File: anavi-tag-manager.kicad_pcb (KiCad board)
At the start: 2 copper layers, 74.9 x 40.6 mm, 31 parts, among them P1 CONN_01X03, U1 I2C_SENS_1, U2 I2C_SENS_1, U3 I2C_SENS_1

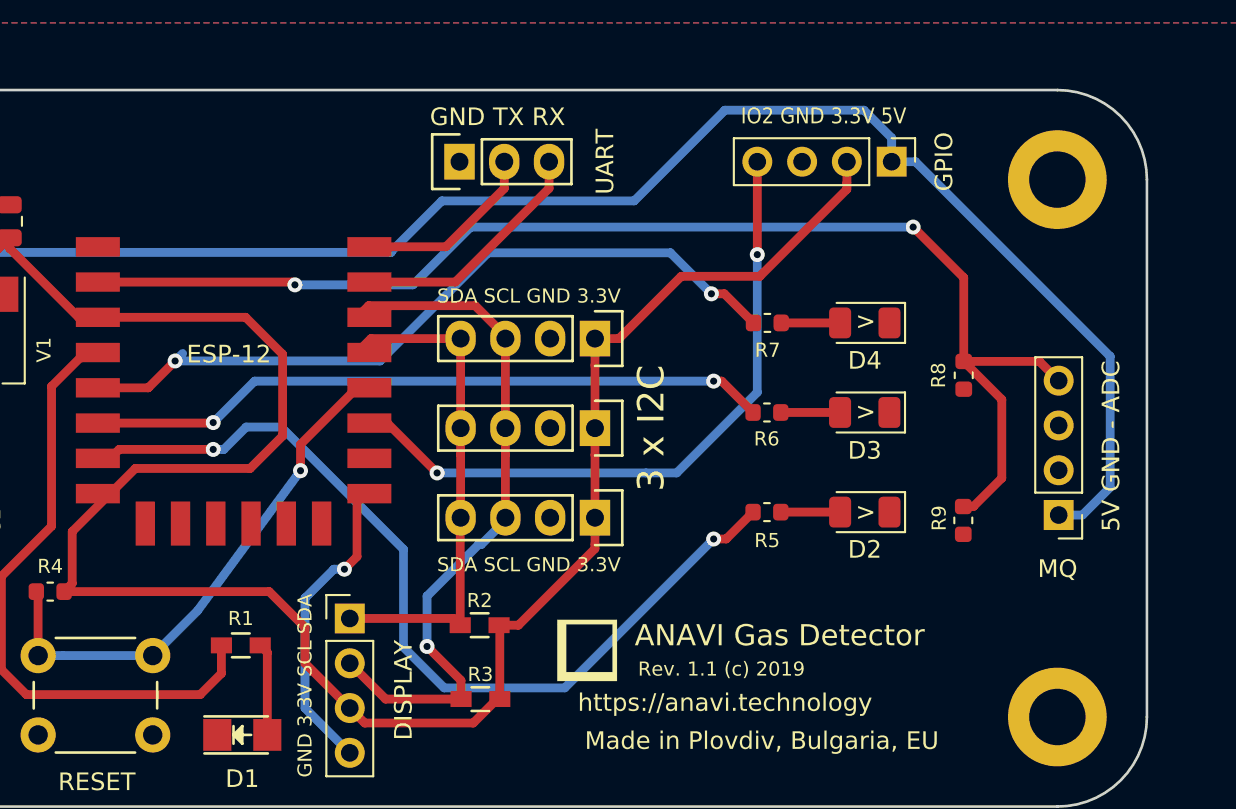
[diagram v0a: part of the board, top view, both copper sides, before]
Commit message: anavi-tag-manager.kicad_pcb: Clear old tracks
Clear old tracks and prepare for net list import.

Signed-off-by: Leon Anavi <leon@anavi.org>
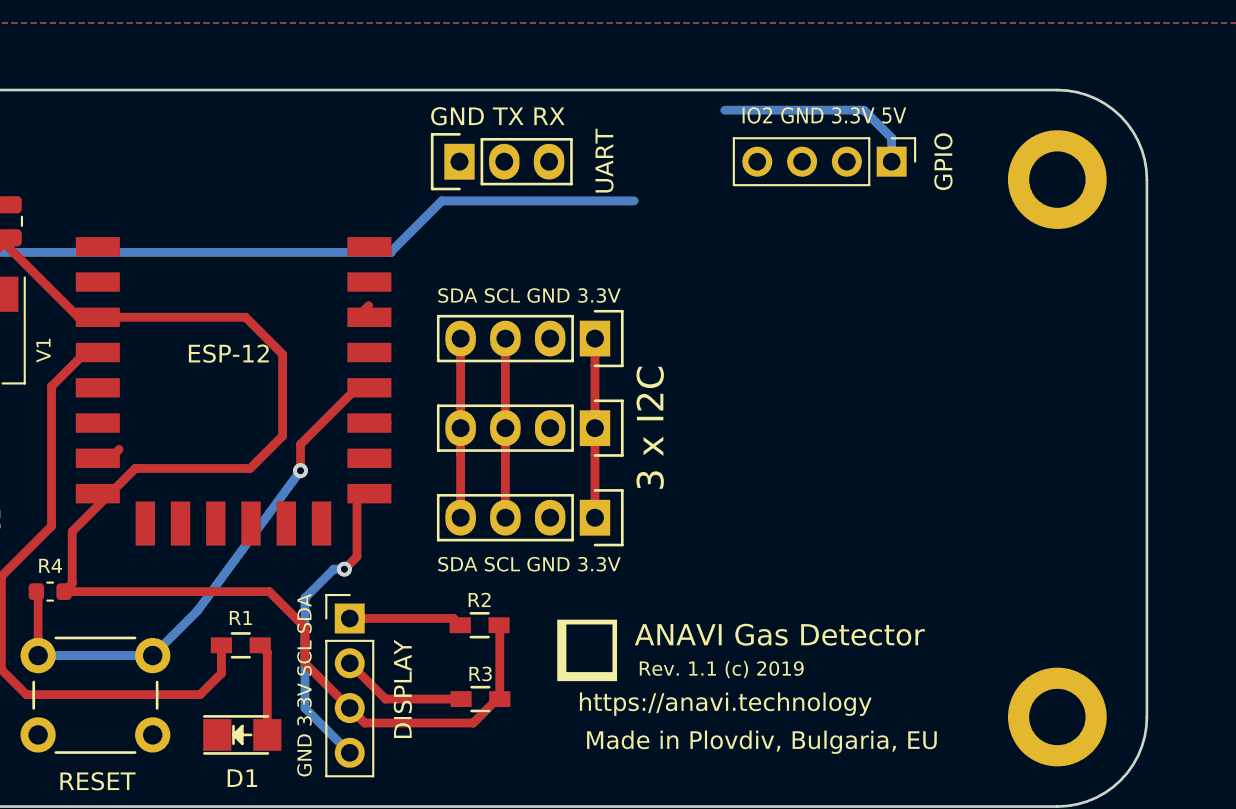
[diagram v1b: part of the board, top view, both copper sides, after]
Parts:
- removed D2: KP-3216SGC, LED_SMD:LED_1206_3216Metric
- removed D3: KP-3216YC, LED_SMD:LED_1206_3216Metric
- removed D4: KP-3216EC, LED_SMD:LED_1206_3216Metric
- removed MQ: Conn_01x04, Connector_PinHeader_2.54mm:PinHeader_1x04_P2.54mm_Vertical
- removed R5, R6, R7: 68R, Resistor_SMD:R_0603_1608Metric
- removed R8: 220K, Resistor_SMD:R_0603_1608Metric
- removed R9: 56K, Resistor_SMD:R_0603_1608Metric
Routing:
- net Net-(ESP-12-Pad2): track 72.0 -> 0.00 mm, vias 2 -> 0
- net Net-(ESP-12-Pad7): track 50.7 -> 0.72 mm, vias 2 -> 0
- net Net-(ESP-12-Pad5): track 41.9 -> 0.00 mm, vias 2 -> 0
- net Net-(ESP-12-Pad6): track 38.2 -> 0.00 mm, vias 2 -> 0
- net Net-(ESP-12-Pad11): track 40.3 -> 3.12 mm, vias 2 -> 0
- net +5V: track 109.3 -> 74.0 mm
- net +3V3: track 118.7 -> 90.3 mm
- net Net-(ESP-12-Pad14): track 39.9 -> 18.5 mm, vias 1 -> 0
- net Net-(ESP-12-Pad15): track 14.6 -> 0.00 mm
- net Net-(ESP-12-Pad13): track 29.9 -> 17.7 mm
- net Net-(ESP-12-Pad16): track 11.2 -> 0.00 mm
- net Net-(D2-Pad2): track 3.36 -> 0.00 mm
- net Net-(D3-Pad2): track 3.36 -> 0.00 mm
- net Net-(D4-Pad2): track 3.34 -> 0.00 mm
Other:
- board text removed: "5V GND - ADC"
- board text removed: ">"

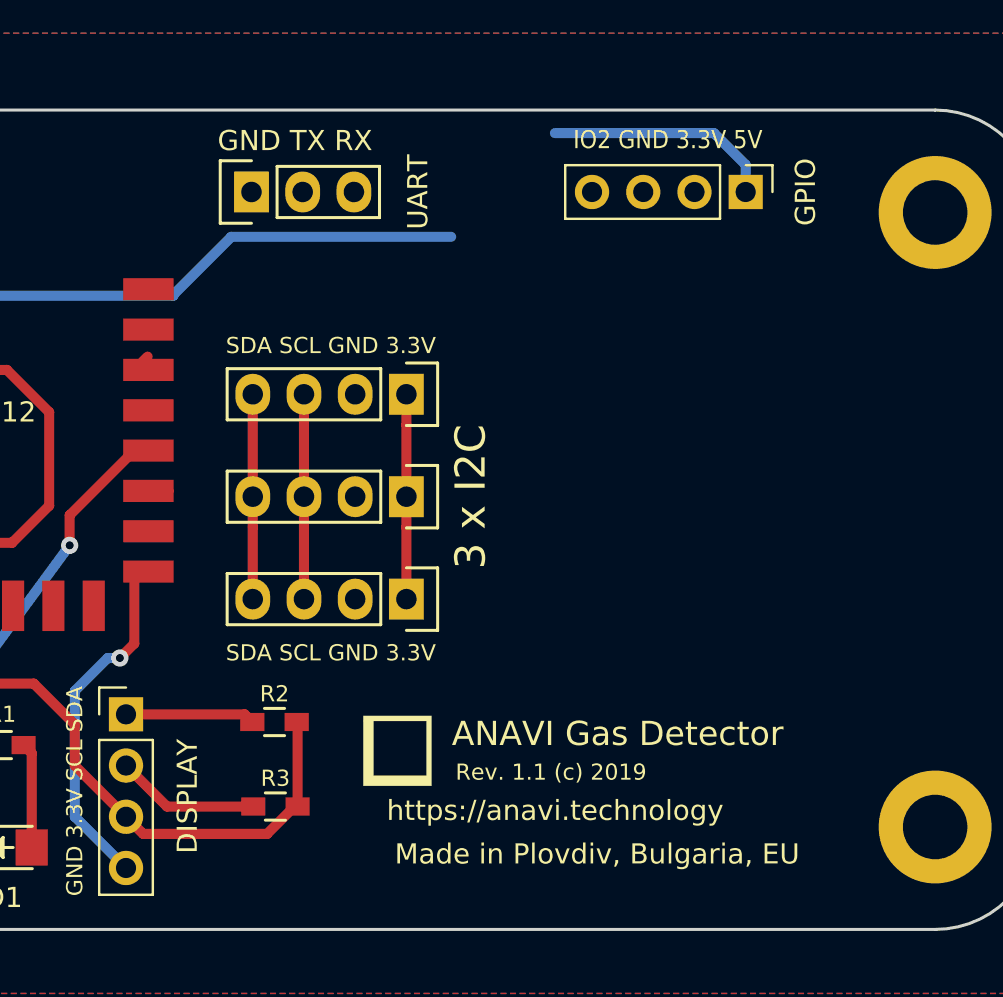
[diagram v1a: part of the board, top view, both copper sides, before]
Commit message: anavi-tag-manager.kicad_pcb: Move components
Move I2C slots and GPIO pins to save some space.

Signed-off-by: Leon Anavi <leon@anavi.org>
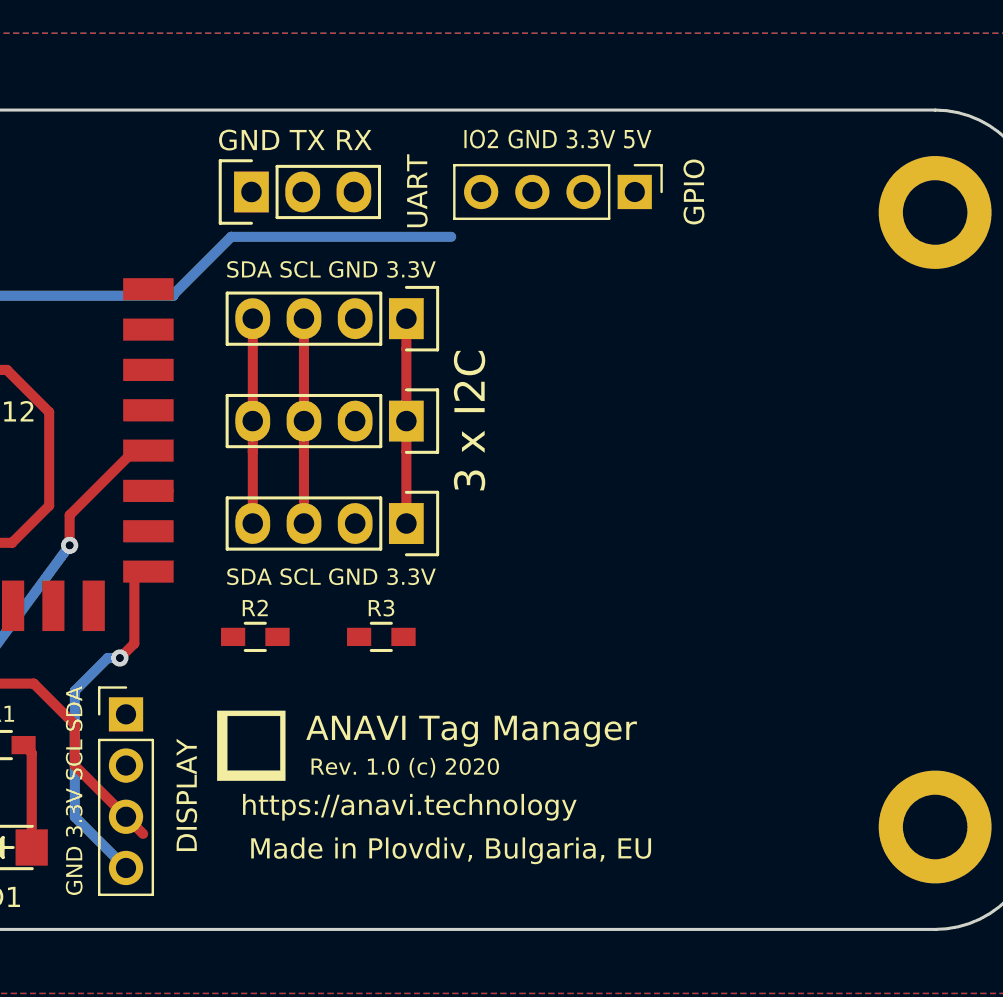
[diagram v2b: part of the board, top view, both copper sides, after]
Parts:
- moved R3 9.92 mm to (107.2, 97.2)
- moved G*** 7.25 mm to (100.7, 102.7)
- moved GPIO 5.50 mm to (119.7, 75.2)
- moved R2 4.33 mm to (100.9, 97.2)
- moved U1 3.75 mm to (108.4, 91.6)
- moved U2 3.75 mm to (108.4, 86.5)
- moved U3 3.75 mm to (108.4, 81.5)
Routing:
- net +3V3: track 90.3 -> 77.9 mm
- net +5V: track 74.0 -> 62.6 mm
- net Net-(ESP-12-Pad14): track 18.5 -> 10.5 mm
- net Net-(ESP-12-Pad13): track 17.7 -> 11.2 mm
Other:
- board text added: "ANAVI Tag Manager"
- board text added: "Rev. 1.0 (c) 2020"
- board text removed: "ANAVI Gas Detector"
- board text removed: "Rev. 1.1 (c) 2019"
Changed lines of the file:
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@@
     (thickness 1.6)
     (drawings 21)
-    (tracks 100)
+    (tracks 87)
     (zones 0)
     (modules 22)
@@
   )
   (setup
-    (last_trace_width 0.5)
+    (last_trace_width 0.254)
     (user_trace_width 0.254)
     (user_trace_width 0.5)
@@
   )
   (module Pin_Headers:Pin_Header_Straight_1x04 (layer F.Cu)
-    (at 108.3945 85.217 270)
+    (at 108.3945 81.467 270)
     (descr "Through hole pin header")
     (tags "pin header")
@@
   )
   (module Resistors_SMD:R_0603_HandSoldering (layer F.Cu)
-    (at 101.854 101.473 180)
+    (at 100.9 97.25 180)
     (descr "Resistor SMD 0603, hand soldering")
     (tags "resistor 0603")
@@
   )
   (module Resistors_SMD:R_0603_HandSoldering (layer F.Cu)
-    (at 101.897 105.664 180)
+    (at 107.15 97.25 180)
     (descr "Resistor SMD 0603, hand soldering")
     (tags "resistor 0603")
@@
   )
   (module Pin_Headers:Pin_Header_Straight_1x04 (layer F.Cu)
-    (at 108.3945 95.377 270)
+    (at 108.3945 91.627 270)
     (descr "Through hole pin header")
     (tags "pin header")
@@
   )
   (module Pin_Headers:Pin_Header_Straight_1x04 (layer F.Cu)
-    (at 108.3945 90.297 270)
+    (at 108.3945 86.547 270)
     (descr "Through hole pin header")
     (tags "pin header")
@@
   )
   (module logo:anavi-logo (layer F.Cu)
-    (at 107.95 102.9462)
+    (at 100.7 102.6962)
     (fp_text reference G*** (at 0 0) (layer F.SilkS) hide
       (effects (font (size 1.524 1.524) (thickness 0.3)))
@@
   )
   (module Connector_PinHeader_2.54mm:PinHeader_1x04_P2.54mm_Vertical (layer F.Cu)
-    (at 125.222 75.184 270)
+    (at 119.722 75.184 270)
     (descr "Through hole straight pin header, 1x04, 2.54mm pitch, single row")
     (tags "Through hole pin header THT 1x04 2.54mm single row")
@@
     )
   )
-  (gr_text "IO2 GND 3.3V 5V" (at 121.3612 72.5932) (layer F.SilkS)
+  (gr_text "IO2 GND 3.3V 5V" (at 115.8612 72.5932) (layer F.SilkS)
     (effects (font (size 0.9 0.8) (thickness 0.15)))
   )
@@
     (effects (font (size 0.8 0.8) (thickness 0.15)))
   )
-  (gr_text "SDA SCL GND 3.3V" (at 104.648 98.044) (layer F.SilkS)
+  (gr_text "SDA SCL GND 3.3V" (at 104.648 94.294) (layer F.SilkS)
     (effects (font (size 0.8 0.8) (thickness 0.15)))
   )
-  (gr_text "SDA SCL GND 3.3V" (at 104.648 82.804) (layer F.SilkS)
+  (gr_text "SDA SCL GND 3.3V" (at 104.648 79.054) (layer F.SilkS)
     (effects (font (size 0.8 0.8) (thickness 0.15)))
   )
@@
     (effects (font (size 1 1) (thickness 0.2)))
   )
-  (gr_text "3 x I2C" (at 111.5822 90.297 90) (layer F.SilkS)
+  (gr_text "3 x I2C" (at 111.5822 86.547 90) (layer F.SilkS)
     (effects (font (size 1.5 1.5) (thickness 0.25)))
   )
@@
     (effects (font (size 1 1) (thickness 0.15)))
   )
-  (gr_text "Made in Plovdiv, Bulgaria, EU" (at 117.856 108.0262) (layer F.SilkS)
+  (gr_text "Made in Plovdiv, Bulgaria, EU" (at 110.606 107.7762) (layer F.SilkS)
     (effects (font (size 1 1) (thickness 0.2)))
   )
-  (gr_text https://anavi.technology (at 115.7732 105.8672) (layer F.SilkS)
+  (gr_text https://anavi.technology (at 108.5232 105.6172) (layer F.SilkS)
     (effects (font (size 1 1) (thickness 0.15)))
   )
-  (gr_text "Rev. 1.1 (c) 2019" (at 115.57 103.9622) (layer F.SilkS)
+  (gr_text "Rev. 1.0 (c) 2020" (at 108.32 103.7122) (layer F.SilkS)
     (effects (font (size 0.8 0.8) (thickness 0.15)))
   )
-  (gr_text "ANAVI Gas Detector" (at 118.872 102.0572) (layer F.SilkS)
+  (gr_text "ANAVI Tag Manager" (at 111.622 101.8072) (layer F.SilkS)
     (effects (font (size 1.2 1.2) (thickness 0.25)))
   )
@@
   (segment (start 91.948 106.172) (end 94.488 108.712) (width 0.5) (layer B.Cu) (net 2))
   (segment (start 91.948 99.93216) (end 91.948 106.172) (width 0.5) (layer B.Cu) (net 2))
-  (segment (start 108.288 85.1105) (end 108.3945 85.217) (width 0.5) (layer F.Cu) (net 3))
+  (segment (start 108.288 81.3605) (end 108.3945 81.467) (width 0.5) (layer F.Cu) (net 3))
   (segment (start 74.384 79.502) (end 75.184 79.502) (width 0.5) (layer F.Cu) (net 3))
   (segment (start 72.644 82.042) (end 75.184 79.502) (width 0.5) (layer F.Cu) (net 3))
@@
   (segment (start 91.948 103.632) (end 94.488 106.172) (width 0.5) (layer F.Cu) (net 3))
   (segment (start 91.948 101.6) (end 91.948 103.632) (width 0.5) (layer F.Cu) (net 3))
-  (segment (start 108.3945 86.733) (end 108.3945 90.297) (width 0.5) (layer F.Cu) (net 3))
-  (segment (start 108.3945 85.217) (end 108.3945 86.733) (width 0.5) (layer F.Cu) (net 3))
-  (segment (start 108.3945 91.813) (end 108.3945 95.377) (width 0.5) (layer F.Cu) (net 3))
-  (segment (start 108.3945 90.297) (end 108.3945 91.813) (width 0.5) (layer F.Cu) (net 3))
-  (segment (start 108.3945 95.5294) (end 108.3945 95.377) (width 0.5) (layer F.Cu) (net 3))
+  (segment (start 108.3945 82.983) (end 108.3945 86.547) (width 0.5) (layer F.Cu) (net 3))
+  (segment (start 108.3945 81.467) (end 108.3945 82.983) (width 0.5) (layer F.Cu) (net 3))
+  (segment (start 108.3945 88.063) (end 108.3945 91.627) (width 0.5) (layer F.Cu) (net 3))
+  (segment (start 108.3945 86.547) (end 108.3945 88.063) (width 0.5) (layer F.Cu) (net 3))
+  (segment (start 108.3945 91.7794) (end 108.3945 91.627) (width 0.5) (layer F.Cu) (net 3))
   (segment (start 78.283 99.568) (end 78.283 99.619) (width 0.5) (layer F.Cu) (net 3))
   (segment (start 80.899 84.01) (end 88.582 84.01) (width 0.5) (layer F.Cu) (net 3))
@@
   (segment (start 82.326 92.583) (end 80.899 94.01) (width 0.5) (layer F.Cu) (net 3))
   (segment (start 88.8365 92.583) (end 82.326 92.583) (width 0.5) (layer F.Cu) (net 3))
-  (segment (start 102.997 101.516) (end 102.954 101.473) (width 0.5) (layer F.Cu) (net 3))
-  (segment (start 102.997 105.664) (end 102.997 101.516) (width 0.5) (layer F.Cu) (net 3))
-  (segment (start 101.489001 107.021999) (end 102.847 105.664) (width 0.5) (layer F.Cu) (net 3))
-  (segment (start 95.337999 107.021999) (end 101.489001 107.021999) (width 0.5) (layer F.Cu) (net 3))
-  (segment (start 102.847 105.664) (end 102.997 105.664) (width 0.5) (layer F.Cu) (net 3))
   (segment (start 94.488 106.172) (end 95.337999 107.021999) (width 0.5) (layer F.Cu) (net 3))
   (segment (start 79.1045 84.01) (end 80.899 84.01) (width 0.5) (layer F.Cu) (net 3))
@@
   (segment (start 78.744612 96.164388) (end 80.899 94.01) (width 0.5) (layer F.Cu) (net 3))
   (segment (start 78.283 99.568) (end 78.744612 99.106388) (width 0.5) (layer F.Cu) (net 3))
-  (segment (start 100.5635 95.969) (end 100.7745 95.758) (width 0.5) (layer F.Cu) (net 4))
-  (segment (start 100.754 85.1965) (end 100.7745 85.217) (width 0.5) (layer F.Cu) (net 4))
-  (segment (start 100.7745 85.217) (end 100.7745 90.297) (width 0.5) (layer F.Cu) (net 4))
-  (segment (start 100.7745 91.813) (end 100.7745 95.377) (width 0.5) (layer F.Cu) (net 4))
-  (segment (start 100.7745 90.297) (end 100.7745 91.813) (width 0.5) (layer F.Cu) (net 4))
-  (segment (start 100.584 95.5675) (end 100.7745 95.377) (width 0.5) (layer F.Cu) (net 4))
+  (segment (start 100.5635 92.219) (end 100.7745 92.008) (width 0.5) (layer F.Cu) (net 4))
+  (segment (start 100.754 81.4465) (end 100.7745 81.467) (width 0.5) (layer F.Cu) (net 4))
+  (segment (start 100.7745 81.467) (end 100.7745 86.547) (width 0.5) (layer F.Cu) (net 4))
+  (segment (start 100.7745 88.063) (end 100.7745 91.627) (width 0.5) (layer F.Cu) (net 4))
+  (segment (start 100.7745 86.547) (end 100.7745 88.063) (width 0.5) (layer F.Cu) (net 4))
+  (segment (start 100.584 91.8175) (end 100.7745 91.627) (width 0.5) (layer F.Cu) (net 4))
   (segment (start 94.8055 100.7745) (end 94.488 101.092) (width 0.5) (layer F.Cu) (net 4))
-  (segment (start 100.373 101.092) (end 100.754 101.473) (width 0.5) (layer F.Cu) (net 4))
-  (segment (start 94.488 101.092) (end 100.373 101.092) (width 0.5) (layer F.Cu) (net 4))
-  (segment (start 100.754 95.3975) (end 100.7745 95.377) (width 0.5) (layer F.Cu) (net 4))
-  (segment (start 95.5589 83.3501) (end 94.899 84.01) (width 0.5) (layer F.Cu) (net 5))
-  (segment (start 103.3145 85.0646) (end 103.3145 85.217) (width 0.5) (layer F.Cu) (net 5))
-  (segment (start 103.3145 85.217) (end 103.3145 90.297) (width 0.5) (layer F.Cu) (net 5))
-  (segment (start 103.3145 91.813) (end 103.3145 95.377) (width 0.5) (layer F.Cu) (net 5))
-  (segment (start 103.3145 90.297) (end 103.3145 91.813) (width 0.5) (layer F.Cu) (net 5))
-  (segment (start 96.52 105.664) (end 100.797 105.664) (width 0.5) (layer F.Cu) (net 5))
-  (segment (start 94.488 103.632) (end 96.52 105.664) (width 0.5) (layer F.Cu) (net 5))
-  (segment (start 103.3145 95.5294) (end 103.3145 95.377) (width 0.5) (layer B.Cu) (net 5))
+  (segment (start 100.754 91.6475) (end 100.7745 91.627) (width 0.5) (layer F.Cu) (net 4))
+  (segment (start 103.3145 81.3146) (end 103.3145 81.467) (width 0.5) (layer F.Cu) (net 5))
+  (segment (start 103.3145 81.467) (end 103.3145 86.547) (width 0.5) (layer F.Cu) (net 5))
+  (segment (start 103.3145 88.063) (end 103.3145 91.627) (width 0.5) (layer F.Cu) (net 5))
+  (segment (start 103.3145 86.547) (end 103.3145 88.063) (width 0.5) (layer F.Cu) (net 5))
+  (segment (start 103.3145 91.7794) (end 103.3145 91.627) (width 0.5) (layer B.Cu) (net 5))
   (segment (start 87.208 104.2064) (end 87.208 102.616) (width 0.5) (layer F.Cu) (net 9))
   (segment (start 86.0044 105.41) (end 87.208 104.2064) (width 0.5) (layer F.Cu) (net 9))
@@
   (segment (start 68.072 90.073) (end 72.644 94.645) (width 0.5) (layer F.Cu) (net 11))
   (segment (start 68.072 85.224) (end 68.072 90.073) (width 0.5) (layer F.Cu) (net 11))
-  (segment (start 125.222 73.834) (end 123.651 72.263) (width 0.5) (layer B.Cu) (net 11))
-  (segment (start 125.222 75.184) (end 125.222 73.834) (width 0.5) (layer B.Cu) (net 11))
-  (segment (start 123.651 72.263) (end 115.7605 72.263) (width 0.5) (layer B.Cu) (net 11))
   (segment (start 110.617 77.4065) (end 99.70928 77.4065) (width 0.5) (layer B.Cu) (net 11))
   (via (at 71.5645 80.3275) (size 0.85) (drill 0.4) (layers F.Cu B.Cu) (net 11))
